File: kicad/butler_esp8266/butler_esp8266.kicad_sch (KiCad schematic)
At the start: 63 parts, among them J1 Conn_02x04_Odd_Even, J3 USB_C_Receptacle_PowerOnly_6P, J4 Screw_Terminal_01x03, J5 Screw_Terminal_01x03, J6 Screw_Terminal_01x03, J7 Screw_Terminal_01x03, J8 Conn_01x02, K1 SANYOU_SRD_Form_C, K2 SANYOU_SRD_Form_C, K3 SANYOU_SRD_Form_C, K4 SANYOU_SRD_Form_C, Q1 BC817, Q2 BC817, Q3 BC817, Q4 BC817, SW1 SW_RST, SW2 SW_Flash, U1 AMS1117-3.3, U2 DS1307Z+, U3 ESP-12F, U4 PC817, U5 PC817, U6 PC817, U7 PC817, Y1 Crystal_Small

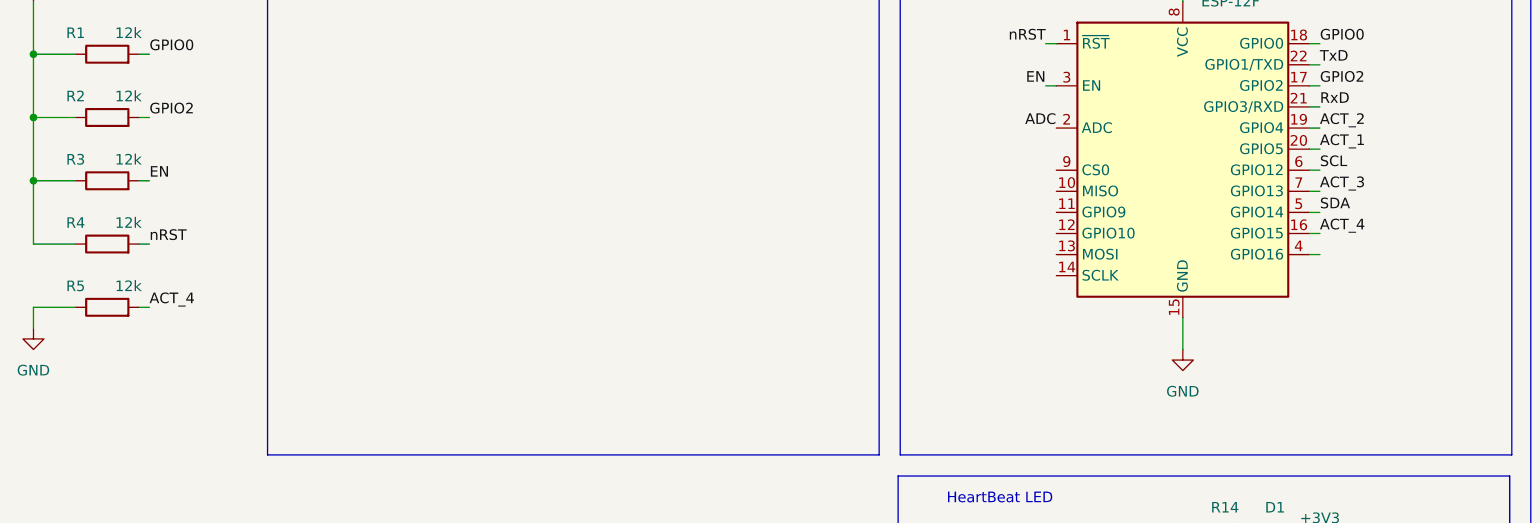
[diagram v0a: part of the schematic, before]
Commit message: Remap 4th actuator to GPIO16 to fix potential unreliability during reboots
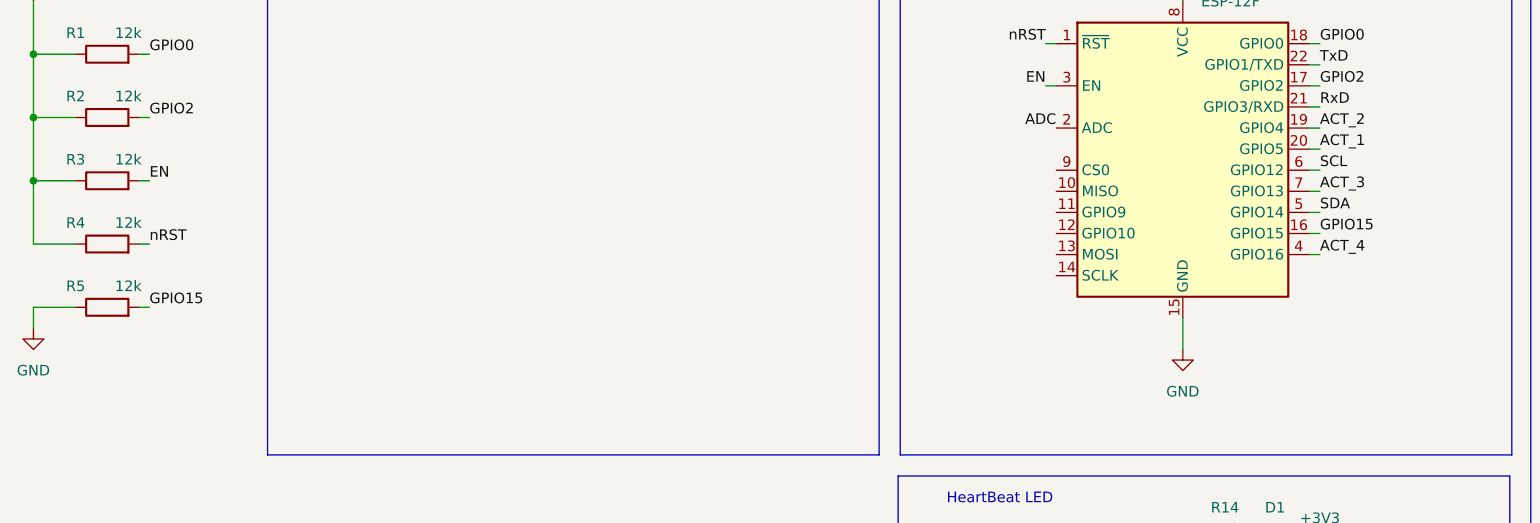
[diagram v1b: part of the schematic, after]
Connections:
- net ACT_4: now also U3.4 (GPIO16); no longer R5.2, U3.16 (GPIO15)
- new net GPIO15: R5.2, U3.16 (GPIO15)
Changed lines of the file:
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@@
 	(wire
 		(pts
-			(xy 175.26 120.65) (xy 173.99 120.65)
+			(xy 173.99 120.65) (xy 175.26 120.65)
 		)
 		(stroke
@@
 	(wire
 		(pts
+			(xy 175.26 118.11) (xy 173.99 118.11)
+		)
+		(stroke
+			(width 0)
+			(type default)
+		)
+	)
+	(wire
+		(pts
 			(xy 262.89 77.47) (xy 262.89 63.5)
 		)
@@
 		(pts
 			(xy 175.26 95.25) (xy 173.99 95.25)
-		)
-		(stroke
-			(width 0)
-			(type default)
-		)
-	)
-	(wire
-		(pts
-			(xy 175.26 118.11) (xy 173.99 118.11)
 		)
 		(stroke
@@
 		)
 	)
-	(label "ACT_4"
+	(label "GPIO15"
 		(at 34.29 127 0)
 		(effects
@@
 	)
 	(label "ACT_4"
-		(at 175.26 118.11 0)
+		(at 175.26 120.65 0)
 		(effects
 			(font
@@
 		(effects
 			(font
+				(size 1.27 1.27)
+			)
+			(justify left bottom)
+		)
+	)
+	(label "GPIO15"
+		(at 175.26 118.11 0)
+		(effects
+			(font
